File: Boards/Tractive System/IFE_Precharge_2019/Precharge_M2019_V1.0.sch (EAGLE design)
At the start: 21 parts

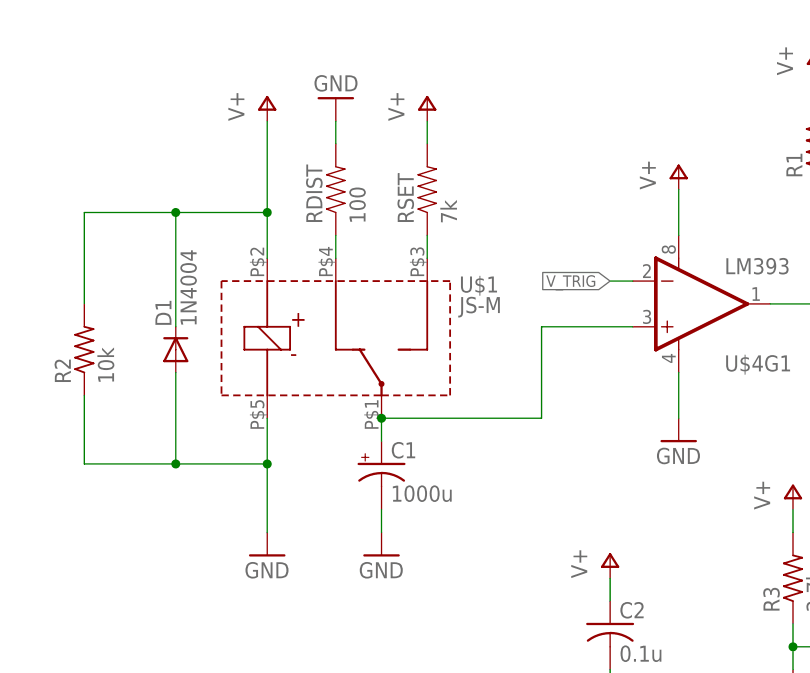
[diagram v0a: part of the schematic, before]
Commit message: Why isnt the gitignore working?! also updated precharge to clean it up a bit
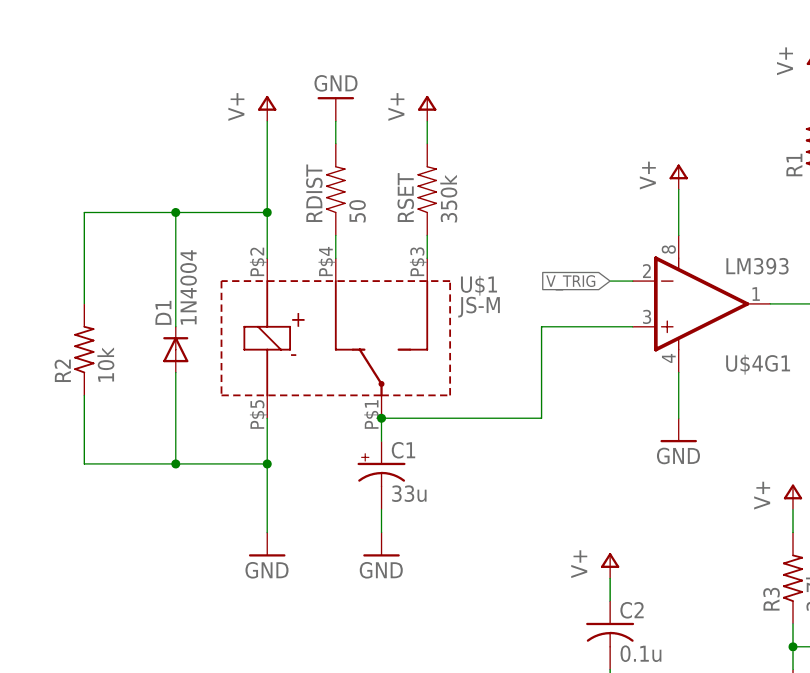
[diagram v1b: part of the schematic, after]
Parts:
- C1: value 1000u -> 33u; device rcl:CPOL-USE5-13 -> rcl:CPOL-USE2.5-5
- RDIST: value 100 -> 50
- RSET: value 7k -> 350k
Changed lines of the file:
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@@
 <parts>
 <part name="U$1" library="Display_Custom" deviceset="JS-M" device=""/>
-<part name="RSET" library="SparkFun-Resistors" deviceset="RESISTOR" device="PTH-1/2W" value="7k"/>
+<part name="RSET" library="SparkFun-Resistors" deviceset="RESISTOR" device="PTH-1/2W" value="350k"/>
 <part name="P+1" library="supply1" library_urn="urn:adsk.eagle:library:371" deviceset="V+" device=""/>
 <part name="P+2" library="supply1" library_urn="urn:adsk.eagle:library:371" deviceset="V+" device=""/>
@@
 <part name="GND2" library="supply1" library_urn="urn:adsk.eagle:library:371" deviceset="GND" device=""/>
 <part name="GND3" library="supply1" library_urn="urn:adsk.eagle:library:371" deviceset="GND" device=""/>
-<part name="C1" library="rcl" library_urn="urn:adsk.eagle:library:334" deviceset="CPOL-US" device="E5-13" package3d_urn="urn:adsk.eagle:package:23375/1" value="1000u"/>
 <part name="D1" library="Diodes_IFE" deviceset="1N4004" device=""/>
 <part name="D2" library="Diodes_IFE" deviceset="1N4004" device=""/>
@@
 <part name="P+11" library="supply1" library_urn="urn:adsk.eagle:library:371" deviceset="V+" device=""/>
 <part name="GND10" library="supply1" library_urn="urn:adsk.eagle:library:371" deviceset="GND" device=""/>
-<part name="RDIST" library="SparkFun-Resistors" deviceset="RESISTOR" device="PTH-1/2W" value="100"/>
+<part name="RDIST" library="SparkFun-Resistors" deviceset="RESISTOR" device="PTH-1/2W" value="50"/>
+<part name="C1" library="rcl" library_urn="urn:adsk.eagle:library:334" deviceset="CPOL-US" device="E2.5-5" package3d_urn="urn:adsk.eagle:package:23344/1" value="33u"/>
 </parts>
 <sheets>
@@
 <instance part="GND2" gate="1" x="60.96" y="17.78"/>
 <instance part="GND3" gate="1" x="55.88" y="68.58" rot="R180"/>
-<instance part="C1" gate="G$1" x="60.96" y="27.94"/>
 <instance part="D1" gate="1" x="38.1" y="40.64" rot="R90"/>
 <instance part="D2" gate="1" x="134.62" y="63.5" rot="R90"/>
@@
 <instance part="GND10" gate="1" x="-7.62" y="40.64"/>
 <instance part="RDIST" gate="G$1" x="55.88" y="58.42" rot="R90"/>
+<instance part="C1" gate="G$1" x="60.96" y="27.94"/>
 </instances>
 <busses>
@@
 <pinref part="U$1" gate="G$1" pin="COM"/>
 <wire x1="60.96" y1="33.02" x2="60.96" y2="30.48" width="0.1524" layer="91"/>
-<pinref part="C1" gate="G$1" pin="+"/>
 <wire x1="60.96" y1="33.02" x2="78.74" y2="33.02" width="0.1524" layer="91"/>
 <junction x="60.96" y="33.02"/>
@@
 <wire x1="78.74" y1="33.02" x2="78.74" y2="43.18" width="0.1524" layer="91"/>
 <wire x1="78.74" y1="43.18" x2="88.9" y2="43.18" width="0.1524" layer="91"/>
+<pinref part="C1" gate="G$1" pin="+"/>
 </segment>
 </net>
@@
 </segment>
 <segment>
-<pinref part="C1" gate="G$1" pin="-"/>
 <pinref part="GND2" gate="1" pin="GND"/>
 <wire x1="60.96" y1="22.86" x2="60.96" y2="20.32" width="0.1524" layer="91"/>
-</segment>
-<segment>
+<pinref part="C1" gate="G$1" pin="-"/>
+</segment>
+<segment>

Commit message: More precharge organization
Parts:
- RSET: value 350k -> 220k; device SparkFun-Resistors:RESISTORPTH-1/2W -> rcl:R-US_0207/10
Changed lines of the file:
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@@
 <parts>
 <part name="U$1" library="Display_Custom" deviceset="JS-M" device=""/>
-<part name="RSET" library="SparkFun-Resistors" deviceset="RESISTOR" device="PTH-1/2W" value="350k"/>
 <part name="P+1" library="supply1" library_urn="urn:adsk.eagle:library:371" deviceset="V+" device=""/>
 <part name="P+2" library="supply1" library_urn="urn:adsk.eagle:library:371" deviceset="V+" device=""/>
@@
 <part name="RDIST" library="SparkFun-Resistors" deviceset="RESISTOR" device="PTH-1/2W" value="50"/>
 <part name="C1" library="rcl" library_urn="urn:adsk.eagle:library:334" deviceset="CPOL-US" device="E2.5-5" package3d_urn="urn:adsk.eagle:package:23344/1" value="33u"/>
+<part name="RSET" library="rcl" library_urn="urn:adsk.eagle:library:334" deviceset="R-US_" device="0207/10" package3d_urn="urn:adsk.eagle:package:23491/1" value="220k"/>
 </parts>
 <sheets>
@@
 <instances>
 <instance part="U$1" gate="G$1" x="53.34" y="43.18"/>
-<instance part="RSET" gate="G$1" x="66.04" y="58.42" rot="R90"/>
 <instance part="P+1" gate="1" x="48.26" y="68.58"/>
 <instance part="P+2" gate="1" x="66.04" y="68.58"/>
@@
 <instance part="RDIST" gate="G$1" x="55.88" y="58.42" rot="R90"/>
 <instance part="C1" gate="G$1" x="60.96" y="27.94"/>
+<instance part="RSET" gate="G$1" x="66.04" y="58.42" rot="R90"/>
 </instances>
 <busses>
@@
 <segment>
 <pinref part="P+2" gate="1" pin="V+"/>
+<wire x1="66.04" y1="66.04" x2="66.04" y2="63.5" width="0.1524" layer="91"/>
 <pinref part="RSET" gate="G$1" pin="2"/>
-<wire x1="66.04" y1="66.04" x2="66.04" y2="63.5" width="0.1524" layer="91"/>
 </segment>
 <segment>
@@
 <net name="N$1" class="0">
 <segment>
-<pinref part="RSET" gate="G$1" pin="1"/>
 <pinref part="U$1" gate="G$1" pin="NO"/>
 <wire x1="66.04" y1="53.34" x2="66.04" y2="50.8" width="0.1524" layer="91"/>
+<pinref part="RSET" gate="G$1" pin="1"/>
 </segment>
 </net>

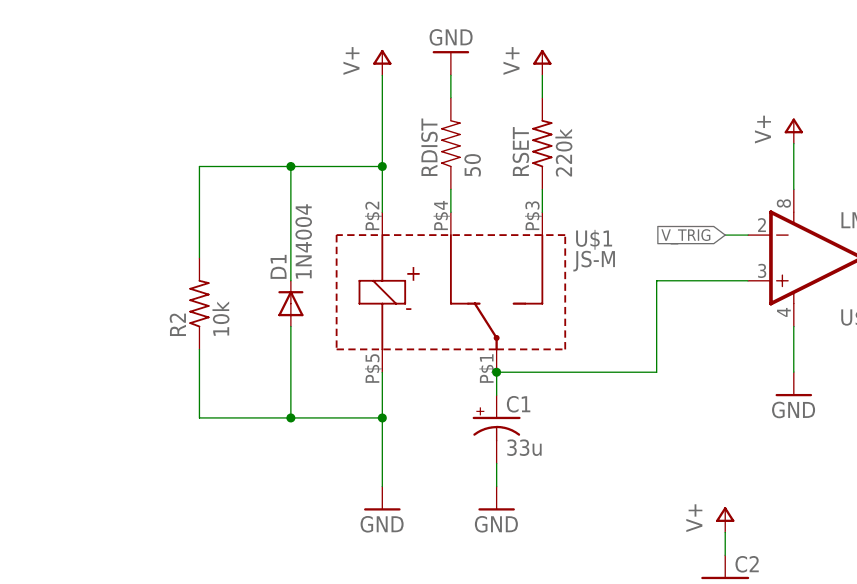
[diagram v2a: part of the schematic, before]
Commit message: Adjusted precharge relay package, reduced area
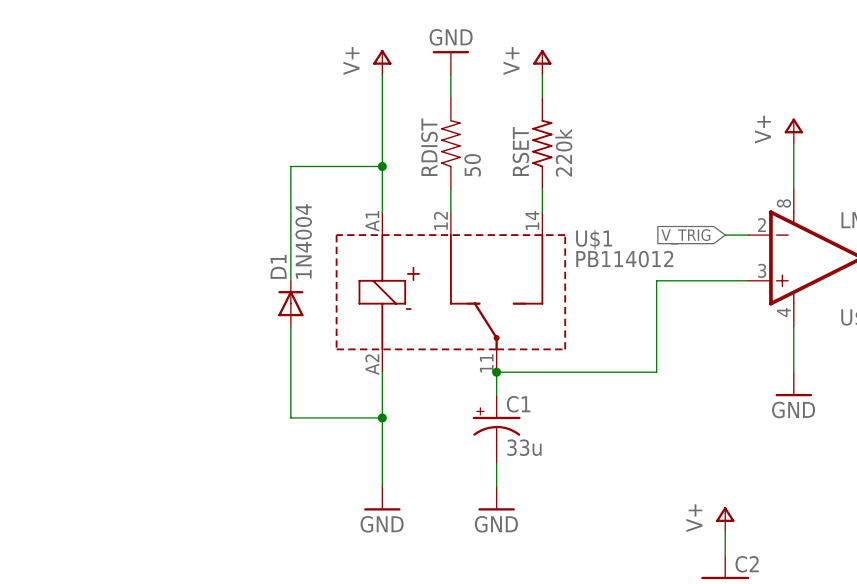
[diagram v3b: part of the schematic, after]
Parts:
- removed R2: 10k, rcl:R-US_R0805
- U$1: value JS-M -> PB114012; device Display_Custom:JS-M -> Display_Custom:PB114012
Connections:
- net GND: no longer R2.1
- net V+: no longer R2.2
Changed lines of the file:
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@@
 </classes>
 <parts>
-<part name="U$1" library="Display_Custom" deviceset="JS-M" device=""/>
 <part name="P+1" library="supply1" library_urn="urn:adsk.eagle:library:371" deviceset="V+" device=""/>
 <part name="P+2" library="supply1" library_urn="urn:adsk.eagle:library:371" deviceset="V+" device=""/>
@@
 <part name="GND4" library="supply1" library_urn="urn:adsk.eagle:library:371" deviceset="GND" device=""/>
 <part name="R1" library="rcl" library_urn="urn:adsk.eagle:library:334" deviceset="R-US_" device="R0805" package3d_urn="urn:adsk.eagle:package:23553/2" value="10k"/>
-<part name="R2" library="rcl" library_urn="urn:adsk.eagle:library:334" deviceset="R-US_" device="R0805" package3d_urn="urn:adsk.eagle:package:23553/2" value="10k"/>
 <part name="P+5" library="supply1" library_urn="urn:adsk.eagle:library:371" deviceset="V+" device=""/>
 <part name="U$3" library="Display_Custom" deviceset="NTD20N03L27" device=""/>
@@
 <part name="C1" library="rcl" library_urn="urn:adsk.eagle:library:334" deviceset="CPOL-US" device="E2.5-5" package3d_urn="urn:adsk.eagle:package:23344/1" value="33u"/>
 <part name="RSET" library="rcl" library_urn="urn:adsk.eagle:library:334" deviceset="R-US_" device="0207/10" package3d_urn="urn:adsk.eagle:package:23491/1" value="220k"/>
+<part name="U$1" library="Display_Custom" deviceset="PB114012" device=""/>
 </parts>
 <sheets>
@@
 </plain>
 <instances>
-<instance part="U$1" gate="G$1" x="53.34" y="43.18"/>
 <instance part="P+1" gate="1" x="48.26" y="68.58"/>
 <instance part="P+2" gate="1" x="66.04" y="68.58"/>
@@
 <instance part="GND4" gate="1" x="93.98" y="30.48"/>
 <instance part="R1" gate="G$1" x="109.22" y="63.5" rot="R90"/>
-<instance part="R2" gate="G$1" x="27.94" y="40.64" rot="R90"/>
 <instance part="P+5" gate="1" x="134.62" y="76.2"/>
 <instance part="U$3" gate="G$1" x="132.08" y="48.26"/>
@@
 <instance part="C1" gate="G$1" x="60.96" y="27.94"/>
 <instance part="RSET" gate="G$1" x="66.04" y="58.42" rot="R90"/>
+<instance part="U$1" gate="G$1" x="53.34" y="43.18"/>
 </instances>
 <busses>
@@
 <segment>
 <pinref part="P+1" gate="1" pin="V+"/>
-<pinref part="U$1" gate="G$1" pin="COIL+"/>
 <wire x1="48.26" y1="66.04" x2="48.26" y2="55.88" width="0.1524" layer="91"/>
 <wire x1="48.26" y1="55.88" x2="48.26" y2="50.8" width="0.1524" layer="91"/>
-<wire x1="27.94" y1="45.72" x2="27.94" y2="55.88" width="0.1524" layer="91"/>
-<wire x1="27.94" y1="55.88" x2="38.1" y2="55.88" width="0.1524" layer="91"/>
 <junction x="48.26" y="55.88"/>
 <pinref part="D1" gate="1" pin="C"/>
 <wire x1="38.1" y1="55.88" x2="48.26" y2="55.88" width="0.1524" layer="91"/>
 <wire x1="38.1" y1="43.18" x2="38.1" y2="55.88" width="0.1524" layer="91"/>
-<junction x="38.1" y="55.88"/>
-<pinref part="R2" gate="G$1" pin="2"/>
+<pinref part="U$1" gate="G$1" pin="COIL+"/>
 </segment>
 <segment>
@@
 <net name="N$1" class="0">
 <segment>
-<pinref part="U$1" gate="G$1" pin="NO"/>
 <wire x1="66.04" y1="53.34" x2="66.04" y2="50.8" width="0.1524" layer="91"/>
 <pinref part="RSET" gate="G$1" pin="1"/>
+<pinref part="U$1" gate="G$1" pin="NO"/>
 </segment>
 </net>
 <net name="N$2" class="0">
 <segment>
-<pinref part="U$1" gate="G$1" pin="COM"/>
 <wire x1="60.96" y1="33.02" x2="60.96" y2="30.48" width="0.1524" layer="91"/>
 <wire x1="60.96" y1="33.02" x2="78.74" y2="33.02" width="0.1524" layer="91"/>
-<junction x="60.96" y="33.02"/>
 <pinref part="U$4" gate="G1" pin="+IN"/>
 <wire x1="78.74" y1="33.02" x2="78.74" y2="43.18" width="0.1524" layer="91"/>
 <wire x1="78.74" y1="43.18" x2="88.9" y2="43.18" width="0.1524" layer="91"/>
 <pinref part="C1" gate="G$1" pin="+"/>
+<pinref part="U$1" gate="G$1" pin="COM"/>
+<junction x="60.96" y="33.02"/>
 </segment>
 </net>
@@
 <segment>
 <pinref part="GND1" gate="1" pin="GND"/>
-<pinref part="U$1" gate="G$1" pin="COIL-"/>
 <wire x1="48.26" y1="33.02" x2="48.26" y2="27.94" width="0.1524" layer="91"/>
 <wire x1="48.26" y1="27.94" x2="48.26" y2="20.32" width="0.1524" layer="91"/>
-<wire x1="27.94" y1="35.56" x2="27.94" y2="27.94" width="0.1524" layer="91"/>
-<wire x1="27.94" y1="27.94" x2="38.1" y2="27.94" width="0.1524" layer="91"/>
 <pinref part="D1" gate="1" pin="A"/>
 <wire x1="38.1" y1="38.1" x2="38.1" y2="27.94" width="0.1524" layer="91"/>
 <wire x1="38.1" y1="27.94" x2="48.26" y2="27.94" width="0.1524" layer="91"/>
-<junction x="38.1" y="27.94"/>
 <junction x="48.26" y="27.94"/>
-<pinref part="R2" gate="G$1" pin="1"/>
+<pinref part="U$1" gate="G$1" pin="COIL-"/>
 </segment>
 <segment>
@@
 <net name="N$3" class="0">
 <segment>
-<pinref part="U$1" gate="G$1" pin="NC"/>
 <wire x1="55.88" y1="53.34" x2="55.88" y2="50.8" width="0.1524" layer="91"/>
 <pinref part="RDIST" gate="G$1" pin="1"/>
-</segment>
-</net>
+<pinref part="U$1" gate="G$1" pin="NC"/>
+</segment>
+</net>
